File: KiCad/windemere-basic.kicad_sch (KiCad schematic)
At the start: 60 parts, among them J1 Barrel_Jack, J2 Connector, SW1 Reset Button, U1 L7805, U2 74HC00, U3 WD65C02, U4 28C256, U5 62256, U6 WD65C22, U7 MM74C922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

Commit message: Update windemere-basic.kicad_sch
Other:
- note added: "~{A15}"
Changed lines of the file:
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@@
     (effects (font (size 1.2 1.2)) (justify left bottom))
+  )
+  (text "~{A15}" (at 64.77 121.92 0)
+    (effects (font (size 1.27 1.27)) (justify left bottom))
   )
   (text "Down" (at 82.55 168.91 0)

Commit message: update symbols
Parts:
- added J1, J3: A_40-LC-TT, digikey-footprints:Socket_DIP-40_15.24mm_Conn, symbol dk_Sockets-for-ICs-Transistors:A_40-LC-TT
- added J2, J4: A_28-LC-TT, digikey-footprints:Socket_DIP-28_15.24mm_Conn, symbol dk_Sockets-for-ICs-Transistors:A_28-LC-TT
- renumbered J1 to J5, J2 to J6
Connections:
- no-connect marks 9 -> 145

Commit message: Update windemere-basic.kicad_sch
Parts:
- removed J1, J3: A_40-LC-TT, digikey-footprints:Socket_DIP-40_15.24mm_Conn, symbol dk_Sockets-for-ICs-Transistors:A_40-LC-TT
- removed J2, J4: A_28-LC-TT, digikey-footprints:Socket_DIP-28_15.24mm_Conn, symbol dk_Sockets-for-ICs-Transistors:A_28-LC-TT
- added J? (x2): A_40-LC-TT, digikey-footprints:Socket_DIP-40_15.24mm_Conn, symbol dk_Sockets-for-ICs-Transistors:A_40-LC-TT
- added J? (x2): A_28-LC-TT, digikey-footprints:Socket_DIP-28_15.24mm_Conn, symbol dk_Sockets-for-ICs-Transistors:A_28-LC-TT
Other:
- note added: "Sockets (So they show on BOM)"

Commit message: Cleanup the Schematic
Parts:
- gave numbers to parts that had none: 4
- renumbered J5 to J1, J6 to J2
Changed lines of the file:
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@@
   (symbol (lib_id "dk_Sockets-for-ICs-Transistors:A_40-LC-TT") (at 313.69 82.55 0) (unit 1)
     (in_bom yes) (on_board no) (fields_autoplaced)
-    (property "Reference" "J?" (id 0) (at 313.69 53.34 0))
+    (property "Reference" "J5" (id 0) (at 313.69 53.34 0))
     (property "Value" "A_40-LC-TT" (id 1) (at 313.69 55.88 0))
     (property "Footprint" "digikey-footprints:Socket_DIP-40_15.24mm_Conn" (id 2) (at 318.77 77.47 0)
@@
   (symbol (lib_id "dk_Sockets-for-ICs-Transistors:A_28-LC-TT") (at 297.18 137.16 0) (unit 1)
     (in_bom yes) (on_board no) (fields_autoplaced)
-    (property "Reference" "J?" (id 0) (at 297.18 114.3 0))
+    (property "Reference" "J4" (id 0) (at 297.18 114.3 0))
     (property "Value" "A_28-LC-TT" (id 1) (at 297.18 116.84 0))
     (property "Footprint" "digikey-footprints:Socket_DIP-28_15.24mm_Conn" (id 2) (at 302.26 132.08 0)
@@
   (symbol (lib_id "dk_Sockets-for-ICs-Transistors:A_40-LC-TT") (at 297.18 82.55 0) (unit 1)
     (in_bom yes) (on_board no) (fields_autoplaced)
-    (property "Reference" "J?" (id 0) (at 297.18 53.34 0))
+    (property "Reference" "J3" (id 0) (at 297.18 53.34 0))
     (property "Value" "A_40-LC-TT" (id 1) (at 297.18 55.88 0))
     (property "Footprint" "digikey-footprints:Socket_DIP-40_15.24mm_Conn" (id 2) (at 302.26 77.47 0)
@@
   (symbol (lib_id "dk_Sockets-for-ICs-Transistors:A_28-LC-TT") (at 313.69 137.16 0) (unit 1)
     (in_bom yes) (on_board no) (fields_autoplaced)
-    (property "Reference" "J?" (id 0) (at 313.69 114.3 0))
+    (property "Reference" "J6" (id 0) (at 313.69 114.3 0))
     (property "Value" "A_28-LC-TT" (id 1) (at 313.69 116.84 0))
     (property "Footprint" "digikey-footprints:Socket_DIP-28_15.24mm_Conn" (id 2) (at 318.77 132.08 0)
@@
   (symbol (lib_id "Connector:Barrel_Jack") (at 44.45 143.51 0) (mirror y) (unit 1)
     (in_bom yes) (on_board yes)
-    (property "Reference" "J5" (id 0) (at 43.0022 135.255 0))
+    (property "Reference" "J1" (id 0) (at 43.0022 135.255 0))
     (property "Value" "Barrel_Jack" (id 1) (at 43.0022 137.5664 0))
     (property "Footprint" "Connector_BarrelJack:BarrelJack_Horizontal" (id 2) (at 43.18 144.526 0)
@@
   (symbol (lib_id "Connector_Generic:Conn_02x20_Odd_Even") (at 237.49 127 0) (unit 1)
     (in_bom yes) (on_board yes) (fields_autoplaced)
-    (property "Reference" "J6" (id 0) (at 238.76 97.79 0))
+    (property "Reference" "J2" (id 0) (at 238.76 97.79 0))
     (property "Value" "Connector" (id 1) (at 238.76 100.33 0))
     (property "Footprint" "Connector_PinHeader_2.54mm:PinHeader_2x20_P2.54mm_Vertical" (id 2) (at 237.49 127 0)
@@
     )
     (path "/daa6f6c2-cfca-4765-905e-4d8d46a60a97"
-      (reference "J5") (unit 1) (value "Barrel_Jack") (footprint "Connector_BarrelJack:BarrelJack_Horizontal")
+      (reference "J1") (unit 1) (value "Barrel_Jack") (footprint "Connector_BarrelJack:BarrelJack_Horizontal")
     )
     (path "/e30d07dc-afa8-430e-989b-dd581033395b"
-      (reference "J6") (unit 1) (value "Connector") (footprint "Connector_PinHeader_2.54mm:PinHeader_2x20_P2.54mm_Vertical")
+      (reference "J2") (unit 1) (value "Connector") (footprint "Connector_PinHeader_2.54mm:PinHeader_2x20_P2.54mm_Vertical")
+    )
+    (path "/7fe0e852-8021-4c1f-9da2-eddf8f0d397c"
+      (reference "J3") (unit 1) (value "A_40-LC-TT") (footprint "digikey-footprints:Socket_DIP-40_15.24mm_Conn")
+    )
+    (path "/7bd08119-7966-4e7e-96ea-59dbfa44b0eb"
+      (reference "J4") (unit 1) (value "A_28-LC-TT") (footprint "digikey-footprints:Socket_DIP-28_15.24mm_Conn")
     )
     (path "/749d5478-5876-4686-be3d-710d89412586"
-      (reference "J?") (unit 1) (value "A_40-LC-TT") (footprint "digikey-footprints:Socket_DIP-40_15.24mm_Conn")
-    )
-    (path "/7bd08119-7966-4e7e-96ea-59dbfa44b0eb"
-      (reference "J?") (unit 1) (value "A_28-LC-TT") (footprint "digikey-footprints:Socket_DIP-28_15.24mm_Conn")
-    )
-    (path "/7fe0e852-8021-4c1f-9da2-eddf8f0d397c"
-      (reference "J?") (unit 1) (value "A_40-LC-TT") (footprint "digikey-footprints:Socket_DIP-40_15.24mm_Conn")
+      (reference "J5") (unit 1) (value "A_40-LC-TT") (footprint "digikey-footprints:Socket_DIP-40_15.24mm_Conn")
     )
     (path "/a2f7fab1-691f-45cd-bc24-848befe214b2"
-      (reference "J?") (unit 1) (value "A_28-LC-TT") (footprint "digikey-footprints:Socket_DIP-28_15.24mm_Conn")
+      (reference "J6") (unit 1) (value "A_28-LC-TT") (footprint "digikey-footprints:Socket_DIP-28_15.24mm_Conn")
     )
     (path "/d832226b-fd15-49cd-aac3-b9dce252e558"

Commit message: Update windemere-basic.kicad_sch
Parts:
- added D?: LED_Red, LED_THT:LED_D5.0mm, symbol Device:LED
- added R?: 1K, Resistor_THT:R_Axial_DIN0207_L6.3mm_D2.5mm_P10.16mm_Horizontal, symbol Device:R
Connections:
- net GND: now also U8.10 (DB3), U8.7 (DB0), U8.8 (DB1), U8.9 (DB2), R?.2
- net at BZ1.1 (-): now also U6.17 (PB7); no longer U6.19 (CB2)
- net at U6.10 (PB0): now also U8.11 (DB4); no longer U8.7 (DB0)
- net at U6.11 (PB1): now also U8.12 (DB5); no longer U8.8 (DB1)
- net at U6.12 (PB2): now also U8.13 (DB6); no longer U8.9 (DB2)
- net at U6.13 (PB3): now also U8.14 (DB7); no longer U8.10 (DB3)
- net at U6.14 (PB4): now also U8.4 (RS); no longer U8.11 (DB4)
- net at U6.15 (PB5): now also U8.5 (R/~{W}); no longer U8.12 (DB5)
- net at U6.16 (PB6): now also U8.6 (E); no longer U8.13 (DB6)
- net at U6.7 (PA5): now also D?.2 (A); no longer U8.4 (RS)
- net at U6.8 (PA6): no longer U8.5 (R/~{W})
- net at U6.9 (PA7): no longer U8.6 (E)
- new net: D?.1 (K), R?.1
- no-connect marks 145 -> 146
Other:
- moved on the sheet: BZ1, C10, C11, RV1, U8

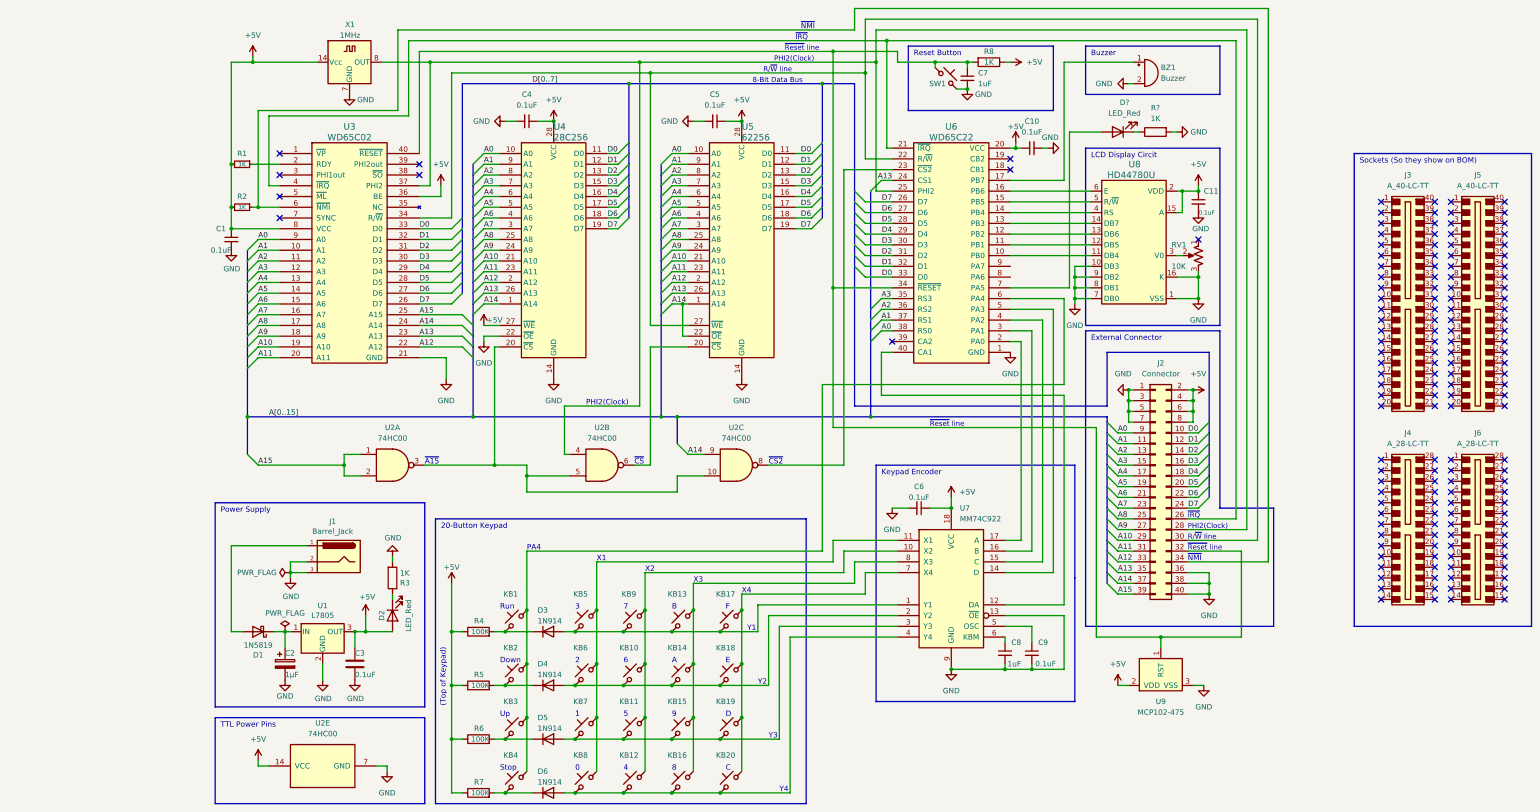
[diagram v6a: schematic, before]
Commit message: Correct buzzer
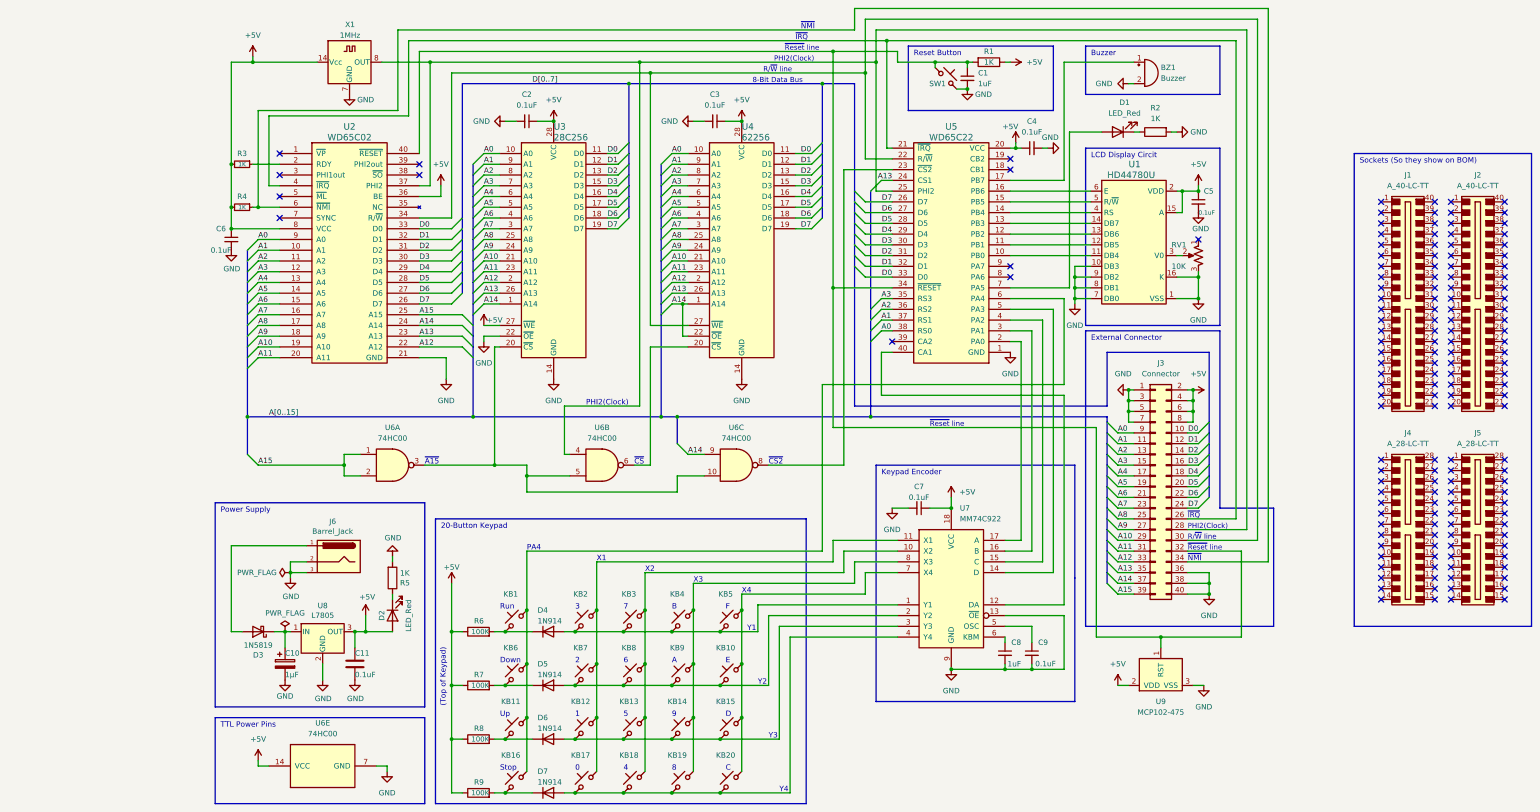
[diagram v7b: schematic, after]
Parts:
- BZ1: Mouser Part (none) -> 490-CEM-1212S
- C1: renamed from C7; Mouser Part (none) -> 80-C322C105K5R9170-R
- C10: renamed from C2; Mouser Part (none) -> 80-ESC105M050AC3AA
- C11: renamed from C3; Mouser Part (none) -> 80-C322C104K5R-TR
- C2: renamed from C4; Mouser Part (none) -> 80-C322C104K5R-TR
- C3: renamed from C5; Mouser Part (none) -> 80-C322C104K5R-TR
- C4: renamed from C10; Mouser Part (none) -> 80-C322C104K5R-TR
- C5: renamed from C11; Mouser Part (none) -> 80-C322C104K5R-TR
- C6: renamed from C1; Mouser Part (none) -> 80-C322C104K5R-TR
- C7: renamed from C6; Mouser Part (none) -> 80-C322C104K5R-TR
- C8: Mouser Part (none) -> 80-C322C105K5R9170-R
- C9: Mouser Part (none) -> 80-C322C104K5R-TR
- D1: renamed from D?; Mouser Part (none) -> 859-LTL-10223W
- D2: Mouser Part (none) -> 859-LTL-10223W
- D3: renamed from D1; Mouser Part (none) -> 863-1N5819G
- D4: renamed from D3; Mouser Part (none) -> 512-1N914
- D5: renamed from D4; Mouser Part (none) -> 512-1N914
- D6: renamed from D5; Mouser Part (none) -> 512-1N914
- D7: renamed from D6; Mouser Part (none) -> 512-1N914
- J1: renamed from J3; Mouser Part (none) -> 517-4840-6004-CP
- J2: renamed from J5; Mouser Part (none) -> 517-4840-6004-CP
- J3: renamed from J2; Mouser Part (none) -> 855-M20-9982045
- J4: Mouser Part (none) -> 517-4828-3004-CP
- J5: renamed from J6; Mouser Part (none) -> 517-4828-3004-CP
- J6: renamed from J1; Mouser Part (none) -> 490-PJ-018H
- KB1, KB20: Mouser Part (none) -> 540-MX1A-11NN
- KB10: renamed from KB18; Mouser Part (none) -> 540-MX1A-11NN
- KB11: renamed from KB3; Mouser Part (none) -> 540-MX1A-11NN
- KB12: renamed from KB7; Mouser Part (none) -> 540-MX1A-11NN
- KB13: renamed from KB11; Mouser Part (none) -> 540-MX1A-11NN
- KB14: renamed from KB15; Mouser Part (none) -> 540-MX1A-11NN
- KB15: renamed from KB19; Mouser Part (none) -> 540-MX1A-11NN
- KB16: renamed from KB4; Mouser Part (none) -> 540-MX1A-11NN
- KB17: renamed from KB8; Mouser Part (none) -> 540-MX1A-11NN
- KB18: renamed from KB12; Mouser Part (none) -> 540-MX1A-11NN
- KB19: renamed from KB16; Mouser Part (none) -> 540-MX1A-11NN
- KB2: renamed from KB5; Mouser Part (none) -> 540-MX1A-11NN
- KB3: renamed from KB9; Mouser Part (none) -> 540-MX1A-11NN
- KB4: renamed from KB13; Mouser Part (none) -> 540-MX1A-11NN
- KB5: renamed from KB17; Mouser Part (none) -> 540-MX1A-11NN
- KB6: renamed from KB2; Mouser Part (none) -> 540-MX1A-11NN
- KB7: renamed from KB6; Mouser Part (none) -> 540-MX1A-11NN
- KB8: renamed from KB10; Mouser Part (none) -> 540-MX1A-11NN
- KB9: renamed from KB14; Mouser Part (none) -> 540-MX1A-11NN
- R1: renamed from R8; Mouser Part (none) -> 660-CFP1/4CT52R102J
- R2: renamed from R?; Mouser Part (none) -> 660-CFP1/4CT52R102J
- R3: renamed from R1; Mouser Part (none) -> 660-CFP1/4CT52R102J
- R4: renamed from R2; Mouser Part (none) -> 660-CFP1/4CT52R102J
- R5: renamed from R3; Mouser Part (none) -> 660-CFP1/4CT52R102J
- R6: renamed from R4; Mouser Part (none) -> 660-CF1/2CT52R104J
- R7: renamed from R5; Mouser Part (none) -> 660-CF1/2CT52R104J
- R8: renamed from R6; Mouser Part (none) -> 660-CF1/2CT52R104J
- R9: renamed from R7; Mouser Part (none) -> 660-CF1/2CT52R104J
- RV1: Mouser Part (none) -> 81-PV36W103C01B00
- SW1: Mouser Part (none) -> 611-D6R90LFS
- U1: renamed from U8; Mouser Part (none) -> 485-181
- U7: Digikey Part MM74C922N-ND -> (none)
- renumbered U3 to U2, U4 to U3, U5 to U4, U6 to U5, U2 to U6, U1 to U8
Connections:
- no-connect marks 146 -> 148

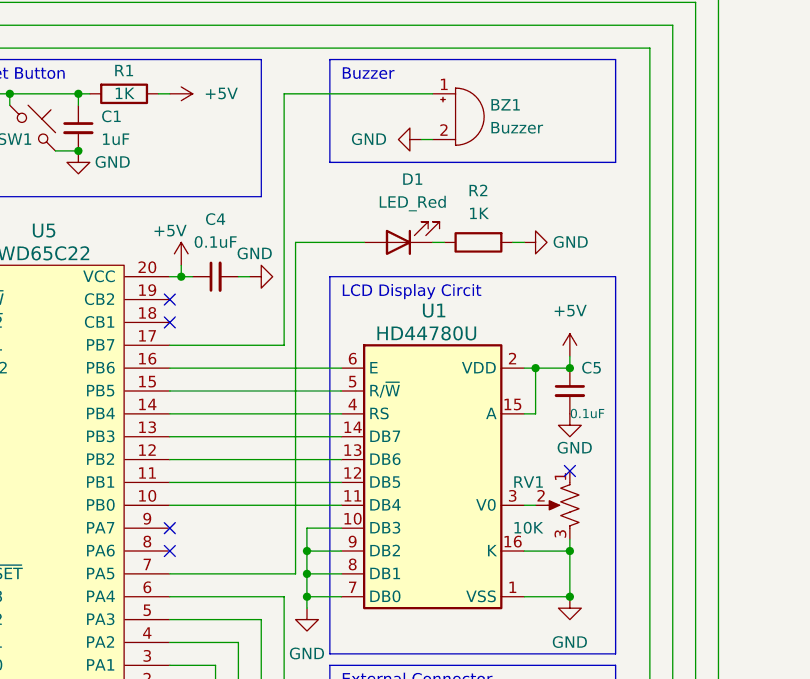
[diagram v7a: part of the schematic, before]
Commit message: correct traces
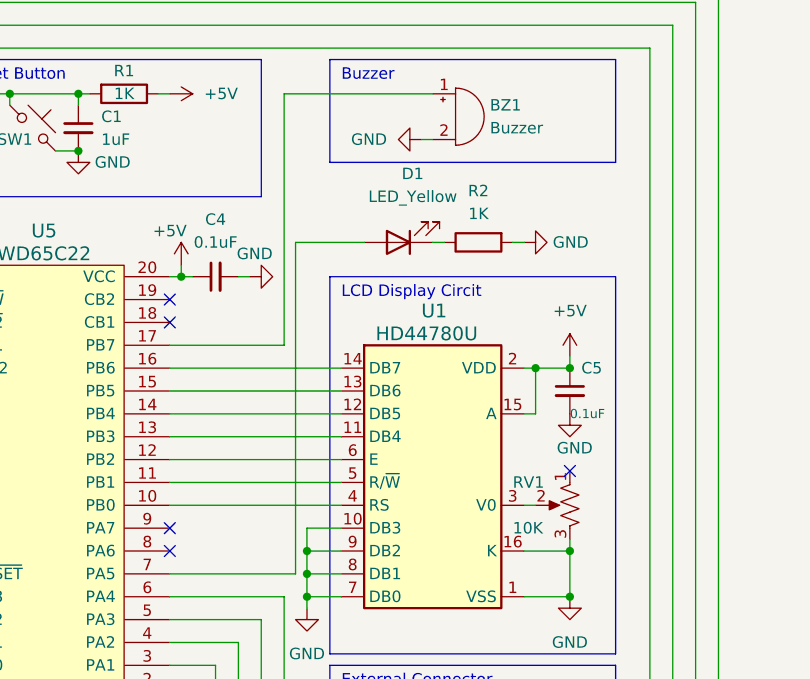
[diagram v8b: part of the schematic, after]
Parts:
- D1: value LED_Red -> LED_Yellow
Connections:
- net at U5.10 (PB0): now also U1.4 (RS); no longer U1.11 (DB4)
- net at U5.11 (PB1): now also U1.5 (R/~{W}); no longer U1.12 (DB5)
- net at U5.12 (PB2): now also U1.6 (E); no longer U1.13 (DB6)
- net at U5.13 (PB3): now also U1.11 (DB4); no longer U1.14 (DB7)
- net at U5.14 (PB4): now also U1.12 (DB5); no longer U1.4 (RS)
- net at U5.15 (PB5): now also U1.13 (DB6); no longer U1.5 (R/~{W})
- net at U5.16 (PB6): now also U1.14 (DB7); no longer U1.6 (E)
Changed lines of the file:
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@@
   (title_block
     (title "Windemere Basic")
-    (date "2022-07-29")
-    (rev "B")
+    (date "2022-07-30")
+    (rev "A")
     (company "Matt Rude <matt@mattrude.com>")
     (comment 1 "65c02 computer with LCD screen and 20 button keypad")
@@
   (symbol (lib_id "Device:LED") (at 228.6 43.18 180) (unit 1)
     (in_bom yes) (on_board yes) (fields_autoplaced)
-    (property "Reference" "D1" (id 0) (at 230.1875 36.195 0))
-    (property "Value" "LED_Red" (id 1) (at 230.1875 38.735 0))
+    (property "Reference" "D1" (id 0) (at 230.1875 35.56 0))
+    (property "Value" "LED_Yellow" (id 1) (at 230.1875 38.1 0))
     (property "Footprint" "LED_THT:LED_D5.0mm" (id 2) (at 228.6 43.18 0)
       (effects (font (size 1.27 1.27)) hide)
@@
     )
     (path "/7a3760ba-c9ab-4fe7-a381-78fdd6e12ae6"
-      (reference "D1") (unit 1) (value "LED_Red") (footprint "LED_THT:LED_D5.0mm")
+      (reference "D1") (unit 1) (value "LED_Yellow") (footprint "LED_THT:LED_D5.0mm")
     )
     (path "/4a170adf-2c48-4dd3-8899-5bdfb579b6d7"
